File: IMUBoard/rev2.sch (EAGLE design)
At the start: 25 parts, among them U1 SAM-M8Q, U2 V_REG_317SMD, U3 MAX3232, U4 OPENIMU

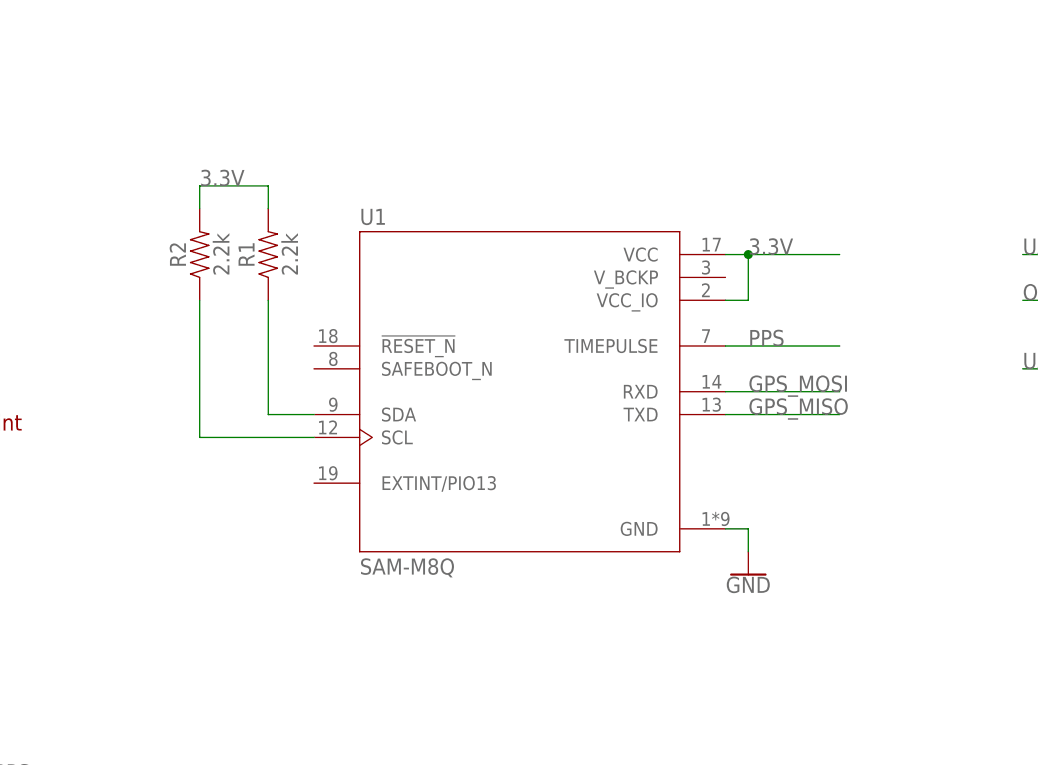
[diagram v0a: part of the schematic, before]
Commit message: IMU board submit, doesn't work
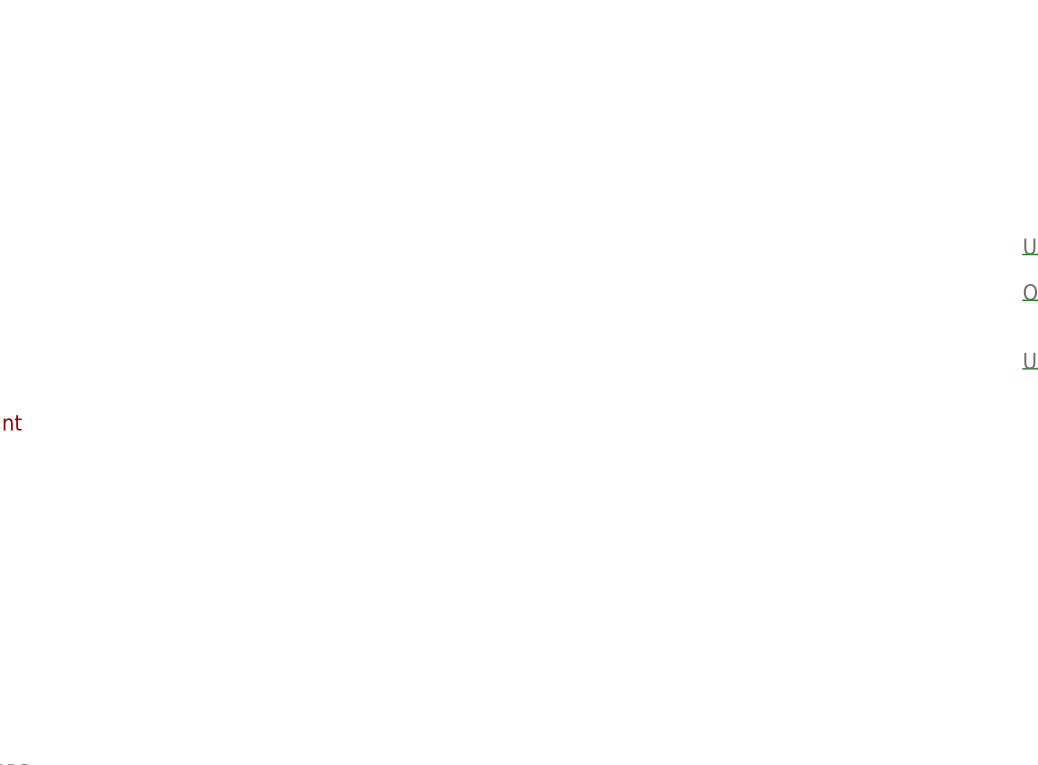
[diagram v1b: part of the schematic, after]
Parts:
- removed R1, R2: 2.2k, SparkFun-Resistors:2.2KOHM-0603-1/10W-1%
- removed U1: SAM-M8Q, SAM-M8Q:SAM-M8Q
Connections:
- removed net N$1: R1.1, U1.SDA
- removed net N$2: R2.1, U1.SCL
- net 3.3V: no longer R1.2, R2.2, U1.VCC, U1.VCC_IO
- net GND: no longer U1.GND
- net GPS_MISO: no longer U1.TXD
- net GPS_MOSI: no longer U1.RXD
- net PPS: no longer U1.TIMEPULSE
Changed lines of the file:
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@@
 </classes>
 <parts>
-<part name="U1" library="SAM-M8Q" deviceset="SAM-M8Q" device=""/>
-<part name="GND1" library="SparkFun-PowerSymbols" deviceset="GND" device=""/>
 <part name="C1" library="SparkFun-Capacitors" deviceset="47UF-POLAR" device="-EIA3528-10V-10%" value="100uF"/>
 <part name="C2" library="SparkFun-Capacitors" deviceset="47UF-POLAR" device="-EIA3528-10V-10%" value="100uF"/>
@@
 <part name="U2" library="SparkFun-IC-Power" deviceset="V_REG_317" device="SMD"/>
 <part name="GND2" library="SparkFun-PowerSymbols" deviceset="GND" device=""/>
-<part name="R1" library="SparkFun-Resistors" deviceset="2.2KOHM" device="-0603-1/10W-1%" value="2.2k"/>
-<part name="R2" library="SparkFun-Resistors" deviceset="2.2KOHM" device="-0603-1/10W-1%" value="2.2k"/>
 <part name="R3" library="SparkFun-Resistors" deviceset="2.2KOHM" device="-0603-1/10W-1%" value="2.2k"/>
 <part name="R4" library="SparkFun-Resistors" deviceset="2.2KOHM" device="-0603-1/10W-1%" value="2.2k"/>
@@
 </plain>
 <instances>
-<instance part="U1" gate="G$1" x="101.6" y="83.82" smashed="yes">
-<attribute name="NAME" x="83.82" y="102.362" size="1.778" layer="95"/>
-<attribute name="VALUE" x="83.82" y="63.5" size="1.778" layer="96"/>
-</instance>
-<instance part="GND1" gate="1" x="127" y="63.5" smashed="yes">
-<attribute name="VALUE" x="127" y="63.246" size="1.778" layer="96" align="top-center"/>
-</instance>
 <instance part="C1" gate="G$1" x="86.36" y="33.02" smashed="yes">
 <attribute name="NAME" x="87.376" y="33.655" size="1.778" layer="95" font="vector"/>
@@
 <instance part="GND2" gate="1" x="104.14" y="22.86" smashed="yes">
 <attribute name="VALUE" x="104.14" y="22.606" size="1.778" layer="96" align="top-center"/>
-</instance>
-<instance part="R1" gate="G$1" x="73.66" y="99.06" smashed="yes" rot="R90">
-<attribute name="NAME" x="72.136" y="99.06" size="1.778" layer="95" font="vector" rot="R90" align="bottom-center"/>
-<attribute name="VALUE" x="75.184" y="99.06" size="1.778" layer="96" font="vector" rot="R90" align="top-center"/>
-</instance>
-<instance part="R2" gate="G$1" x="66.04" y="99.06" smashed="yes" rot="R90">
-<attribute name="NAME" x="64.516" y="99.06" size="1.778" layer="95" font="vector" rot="R90" align="bottom-center"/>
-<attribute name="VALUE" x="67.564" y="99.06" size="1.778" layer="96" font="vector" rot="R90" align="top-center"/>
 </instance>
 <instance part="R3" gate="G$1" x="172.72" y="53.34" smashed="yes" rot="R90">
@@
 <net name="PPS" class="0">
 <segment>
-<pinref part="U1" gate="G$1" pin="TIMEPULSE"/>
-<wire x1="124.46" y1="88.9" x2="137.16" y2="88.9" width="0.1524" layer="91"/>
-<label x="127" y="88.9" size="1.778" layer="95"/>
-</segment>
-<segment>
 <pinref part="R4" gate="G$1" pin="2"/>
 <wire x1="182.88" y1="58.42" x2="182.88" y2="63.5" width="0.1524" layer="91"/>
@@
 </net>
 <net name="GND" class="0">
-<segment>
-<pinref part="U1" gate="G$1" pin="GND"/>
-<pinref part="GND1" gate="1" pin="GND"/>
-<wire x1="124.46" y1="68.58" x2="127" y2="68.58" width="0.1524" layer="91"/>
-<wire x1="127" y1="68.58" x2="127" y2="66.04" width="0.1524" layer="91"/>
-</segment>
 <segment>
 <pinref part="C1" gate="G$1" pin="-"/>
@@
 <net name="GPS_MOSI" class="0">
 <segment>
-<pinref part="U1" gate="G$1" pin="RXD"/>
-<wire x1="124.46" y1="83.82" x2="137.16" y2="83.82" width="0.1524" layer="91"/>
-<label x="127" y="83.82" size="1.778" layer="95"/>
-</segment>
-<segment>
 <pinref part="U4" gate="G$1" pin="U2_TX"/>
 <wire x1="10.16" y1="20.32" x2="-5.08" y2="20.32" width="0.1524" layer="91"/>
@@
 </net>
 <net name="GPS_MISO" class="0">
-<segment>
-<pinref part="U1" gate="G$1" pin="TXD"/>
-<wire x1="124.46" y1="81.28" x2="137.16" y2="81.28" width="0.1524" layer="91"/>
-<label x="127" y="81.28" size="1.778" layer="95"/>
-</segment>
 <segment>
 <pinref part="U4" gate="G$1" pin="U2_RX"/>
@@
 </net>
 <net name="3.3V" class="0">
-<segment>
-<pinref part="U1" gate="G$1" pin="VCC"/>
-<wire x1="124.46" y1="99.06" x2="127" y2="99.06" width="0.1524" layer="91"/>
-<label x="127" y="99.06" size="1.778" layer="95"/>
-<pinref part="U1" gate="G$1" pin="VCC_IO"/>
-<wire x1="127" y1="99.06" x2="137.16" y2="99.06" width="0.1524" layer="91"/>
-<wire x1="124.46" y1="93.98" x2="127" y2="93.98" width="0.1524" layer="91"/>
-<wire x1="127" y1="93.98" x2="127" y2="99.06" width="0.1524" layer="91"/>
-<junction x="127" y="99.06"/>
-</segment>
 <segment>
 <pinref part="U2" gate="G$1" pin="OUT"/>
@@
 </segment>
 <segment>
-<pinref part="R2" gate="G$1" pin="2"/>
-<wire x1="66.04" y1="104.14" x2="66.04" y2="106.68" width="0.1524" layer="91"/>
-<wire x1="66.04" y1="106.68" x2="73.66" y2="106.68" width="0.1524" layer="91"/>
-<pinref part="R1" gate="G$1" pin="2"/>
-<wire x1="73.66" y1="106.68" x2="73.66" y2="104.14" width="0.1524" layer="91"/>
-<label x="66.04" y="106.68" size="1.778" layer="95"/>
-</segment>
-<segment>
 <pinref part="R3" gate="G$1" pin="2"/>
 <wire x1="172.72" y1="58.42" x2="172.72" y2="60.96" width="0.1524" layer="91"/>
@@
 </segment>
 </net>
-<net name="N$1" class="0">
-<segment>
-<pinref part="U1" gate="G$1" pin="SDA"/>
-<pinref part="R1" gate="G$1" pin="1"/>
-<wire x1="78.74" y1="81.28" x2="73.66" y2="81.28" width="0.1524" layer="91"/>
-<wire x1="73.66" y1="81.28" x2="73.66" y2="93.98" width="0.1524" layer="91"/>
-</segment>
-</net>
-<net name="N$2" class="0">
-<segment>
-<pinref part="R2" gate="G$1" pin="1"/>
-<pinref part="U1" gate="G$1" pin="SCL"/>
-<wire x1="66.04" y1="93.98" x2="66.04" y2="78.74" width="0.1524" layer="91"/>
-<wire x1="66.04" y1="78.74" x2="78.74" y2="78.74" width="0.1524" layer="91"/>
-</segment>
-</net>
